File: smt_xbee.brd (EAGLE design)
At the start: 204.4 x 88.6 mm, 134 parts, among them IC1 P82B715D, J1 6473427-1, J2 VR10S05, Q1 MOSFET-NCHANNELSMD, Q2 MOSFET-NCHANNELSMD, SW1 CTS_ELECTROCOMPONENTS_204-211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, SW2 CTS_ELECTROCOMPONENTS_204-211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, U1 XC6220B331MR-G, U4 ARDUINO_R3_SHIELD, U6 ADS1119IPWT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

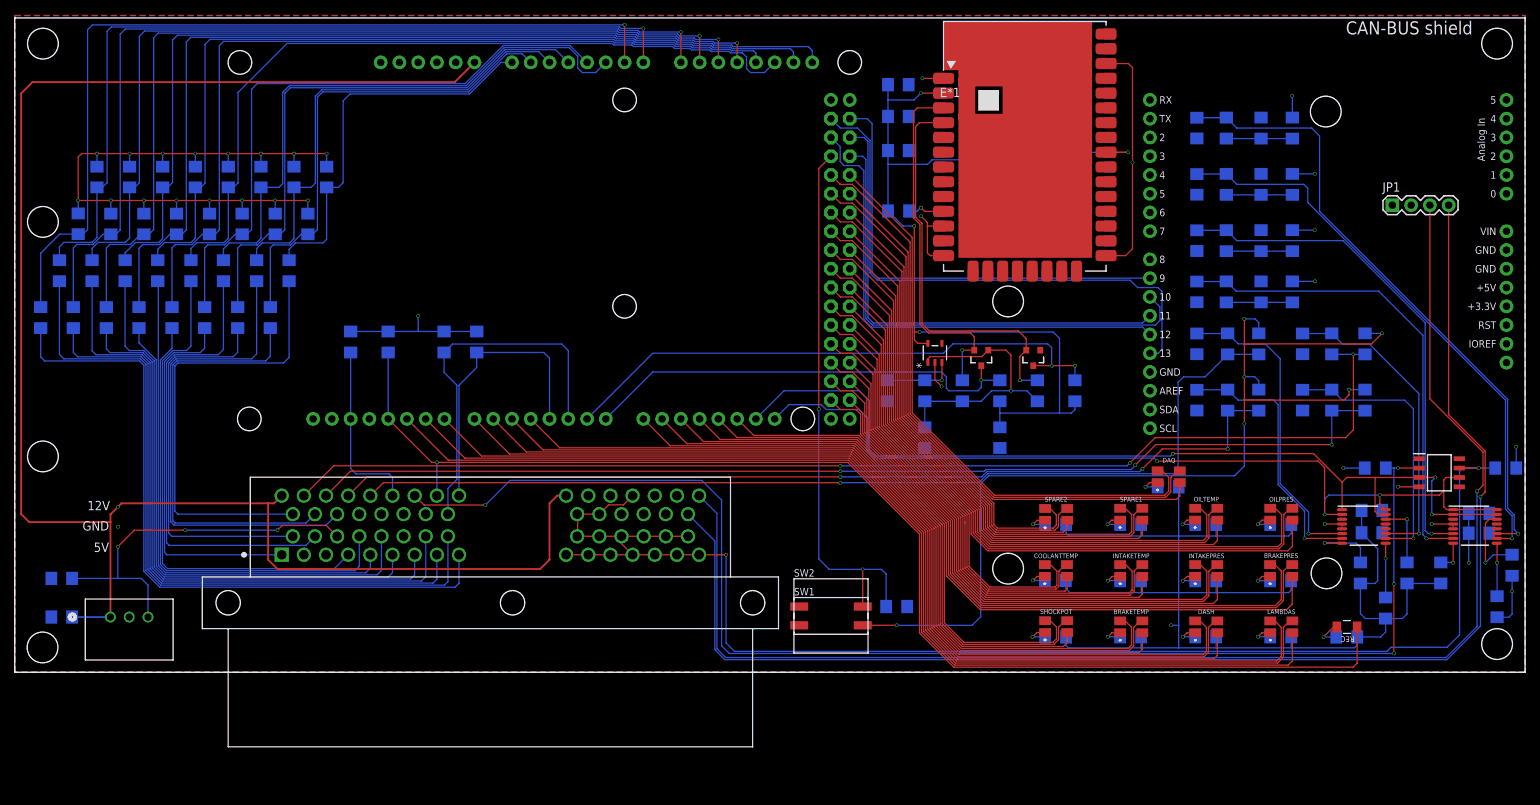
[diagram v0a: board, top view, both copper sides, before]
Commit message: SMT XBee
Added XBee 3D model
Moved connector to be flush with board
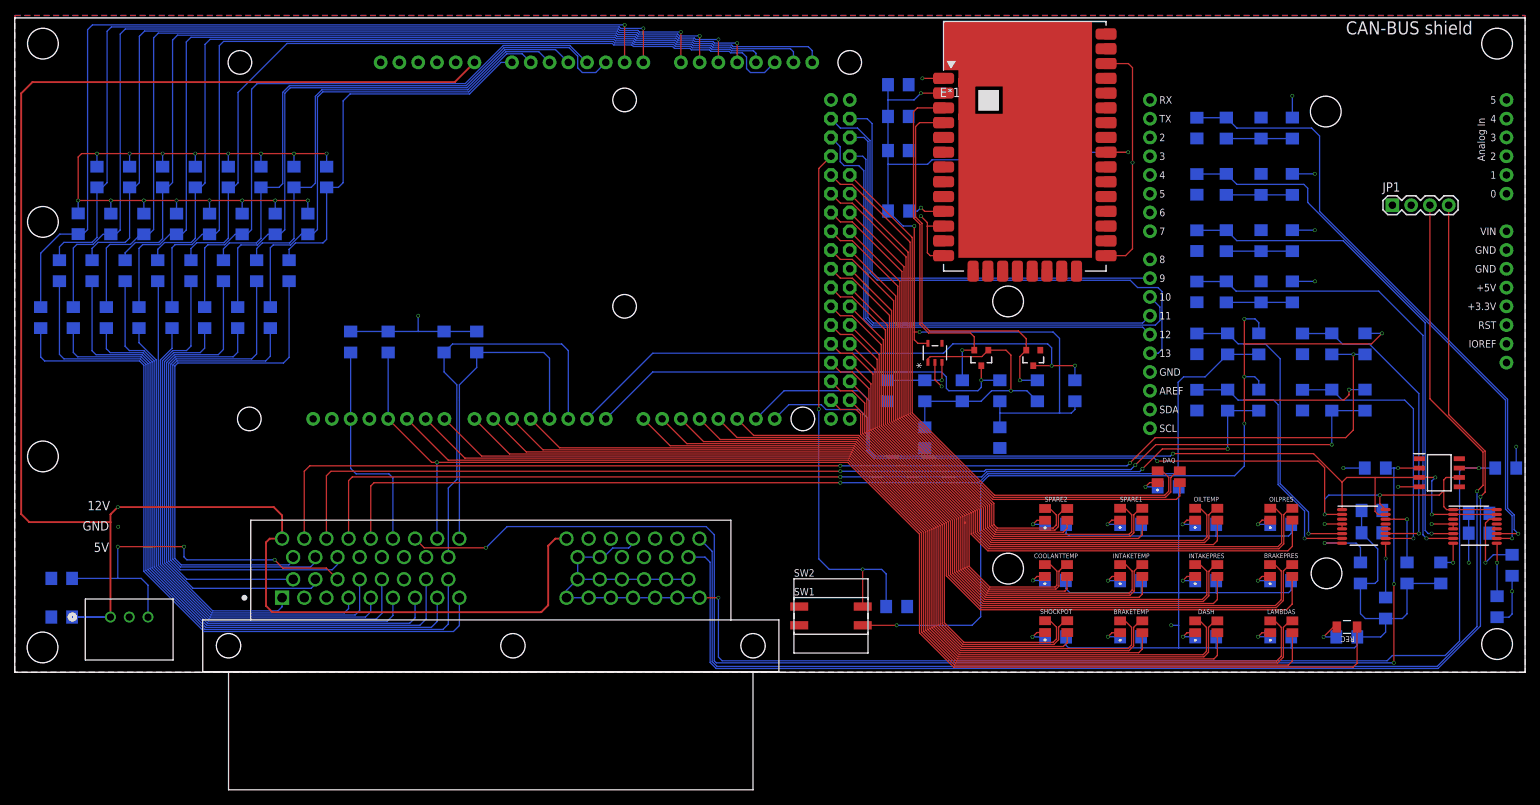
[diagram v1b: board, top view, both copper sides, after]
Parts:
- moved J1 5.82 mm to (53.5, 56.9)
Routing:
- net SG_41: track 160.5 -> 168.2 mm
- net A0IN: track 62.0 -> 69.4 mm
- net SG_31: track 148.1 -> 155.4 mm
- net SG_21: track 131.1 -> 138.0 mm
- net 12V: track 233.0 -> 239.8 mm
- net SG_11: track 135.1 -> 141.6 mm
- net A2IN: track 66.7 -> 73.0 mm
- net A1IN: track 58.5 -> 64.5 mm
- net CALIB: track 24.3 -> 30.2 mm
- net REC: track 171.5 -> 177.4 mm
- net FR_WS: track 38.8 -> 44.6 mm
- net FL_WS: track 50.0 -> 55.8 mm
- net A4IN: track 50.7 -> 56.2 mm
- net A3IN: track 53.2 -> 57.9 mm
- net A5IN: track 62.8 -> 67.2 mm
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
